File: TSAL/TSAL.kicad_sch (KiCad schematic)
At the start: 111 parts, among them IC1 ISO224ADWVR, IC2 ISO224ADWVR, IC3 LTC6995IS6-2#TRMPBF, IC4 LTC6995IS6-2#TRMPBF, J1 Conn_SDC, J2 Conn_TSAL, J3 Conn_AIR, J4 Conn_01x02, J5 Conn_VI, J6 Conn_Control, J7 Conn_HV, J8 Conn_Pre, K1 G2RL-2, Q1 ZXM61N02F, Q2 ZXM61N02F, Q3 ZXM61N02F, Q4 ZXM61N02F, Q5 IXTA6N100D2, U3 TLV7041DBV, U4 TLV7041DBV, U5 74LVC1G08, U6 AP2205-W5-7, U7 AP2205-W5-7, U9 AP2204K-ADJ

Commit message: feat: change iso OPA type and preC. circuit
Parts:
- removed C11: 0.1u, Capacitor_SMD:C_0603_1608Metric, symbol Device:C
- removed C12, C5: 0.22u, Capacitor_SMD:C_0603_1608Metric, symbol Device:C_Small
- removed C13, C18: 0.1u, Capacitor_SMD:C_0603_1608Metric, symbol Device:C_Small
- removed C14, C15, C19, C33: 1u, Capacitor_SMD:C_0603_1608Metric, symbol Device:C_Small
- removed D2: 1SS355VM, Diode_SMD:D_SOD-323F, symbol Diode:1SS355VM
- removed D3: BYG10J, Diode_SMD:D_SMA, symbol Device:D_Zener
- removed IC1, IC2: ISO224ADWVR, Package_SO:SOIC-8_7.5x5.85mm_P1.27mm, symbol ISO224ADWVR:ISO224ADWVR
- removed Q5: IXTA6N100D2, Package_TO_SOT_THT:TO-247-3_Vertical, symbol PCM_Transistor_MOSFET_AKL:IXTA6N100D2
- removed RV2, RV4: 10K, Potentiometer_THT:Potentiometer_Bourns_3296W_Vertical, symbol Device:R_Potentiometer
- removed TP3, TP9: TestPoint, TestPoint:TestPoint_THTPad_D1.5mm_Drill0.7mm, symbol Connector:TestPoint
- added C1, C3: 330p, Capacitor_SMD:C_0603_1608Metric, symbol Device:C_Small
- added C4: 1n, Capacitor_SMD:C_0603_1608Metric, symbol Device:C
- added C5: 1u, Capacitor_SMD:C_0603_1608Metric, symbol Device:C
- added D2: 1N4148W, Diode_SMD:D_SOD-123, symbol Diode:1N4148W
- added D3: S1J, Diode_SMD:D_SMA, symbol PCM_Diode_AKL:S1J
- added F2: 0ACJ-2000-TE, BelFuse:0ACJ, symbol Device:Fuse
- added Q5: DN2470K4, Package_TO_SOT_SMD:TO-252-2, symbol PCM_Transistor_MOSFET_AKL:DN2470K4
- added R1, R2, R3, R4: 3k3, Resistor_SMD:R_0603_1608Metric, symbol Device:R
- added R39, R46, R47, R48, R7: 1M, Resistor_SMD:R_0603_1608Metric, symbol Device:R
- added R5: 100k, Resistor_SMD:R_0603_1608Metric, symbol Device:R
- added TP1: TestPoint, TestPoint:TestPoint_THTPad_D1.5mm_Drill0.7mm, symbol Connector:TestPoint
- added U1, U8: AMC1351, Package_SO:SOIC-8_7.5x5.85mm_P1.27mm, symbol Amplifier_Difference:AMC1100DWV
- added U10, U2: TLV7041DBV, Package_TO_SOT_SMD:SOT-23-5, symbol Comparator:TLV7041DBV
- C10: value 1u -> 0.1u
- C8: value 0.22u -> 1n
- C9: value 0.22u -> 0.1u
- J6: value Conn_Control -> Conn_PRE
- J8: value Conn_Pre -> Conn_control
- Q1, Q2, Q3, Q4: value ZXM61N02F -> 2N7002
- R12, R15: value 82K -> 40k
- R13: value 5.1 -> 20k
- R17: value 5.1 -> 37k
- R20: value 1k -> 3k3
- R22, R23, R24: value 1k -> 1M
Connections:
- net +5V: now also R7.1, U1.8 (V+), U2.5 (V+), U8.8 (V+); no longer R23.1
- net +5VA: now also C9.1, C5.1, U1.1 (V+), U10.5 (V+), U8.1 (V+)
- net BATT+: now also F2.2, R39.1; no longer D10.2 (A), J7.4 (Pin_4)
- net GND1: now also R17.2, C4.2, C5.2, U1.3 (-), U1.4 (V-), U10.2 (V-), U8.3 (-), U8.4 (V-)
- net GND2: now also R24.1, C3.2, R4.1, R5.1, U1.5 (V-), U2.2 (V-), U8.5 (V-)
- net SDC: now also D2.1 (K)
- net at U3.3 (+): now also C1.1, R3.2, TP1.1, U2.1; no longer R20.1
- net at TP8.1, U4.1, U5.1: no longer R23.2
- net at J5.1 (Pin_1), R6.1, RV3.2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: now also Q5.1 (G)
- net at D4.2 (A): now also Q5.2 (D)
- net at RV3.1: now also Q5.3 (S)
- net at R21.2, TP7.1, U3.1: no longer R22.2
- net at U4.3 (+): now also R20.2; no longer R24.1
- net at U4.4 (-): now also R22.2, R23.2
- net at R15.2: now also R19.2, U10.3 (+); no longer R17.1
- net at J7.3 (Pin_3): now also D3.2 (A)
- net at R24.2: now also R23.1
- net at U3.4 (-): now also R13.2, R7.2
- net at R12.2: now also C8.1, R11.2, U1.2 (+); no longer R13.1
- net at K1.A2, Q2.3 (D): now also D2.2 (A)
- net BATT-: no longer names the net of D1.1 (K), J7.1 (Pin_1)
- new net: C3.1, R1.2, R4.2, U2.3 (+)
- new net: D3.1 (K), F2.1
- new net: C1.2, R2.2, R3.1, U2.4 (-)
- new net: R46.2, R47.1
- new net: R47.2, R48.1
- new net: D10.2 (A), J7.4 (Pin_4)
- new net: R39.2, R46.1
- new net: R2.1, U1.6 (-)
- new net: R1.1, U1.7 (+)
- new net: C4.1, U10.1, U8.2 (+)
- new net: R20.1, U8.7 (+)
- new net: R17.1, R48.2, U10.4 (-)
- new net: R13.1, R5.2
- no-connect marks 9 -> 8
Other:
- note added: "All resistors accuracy inside must within 1%."
- note added: "Rin=4.039M ->"
- note added: "Rin_{OPA}=1.25M"
- note removed: "Rin=1.25M"
- note removed: "Rtotal=87333"
- moved on the sheet: C17, C21, C6, C7, C8, D6, J2, J4, Q1, R10, R11, R12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

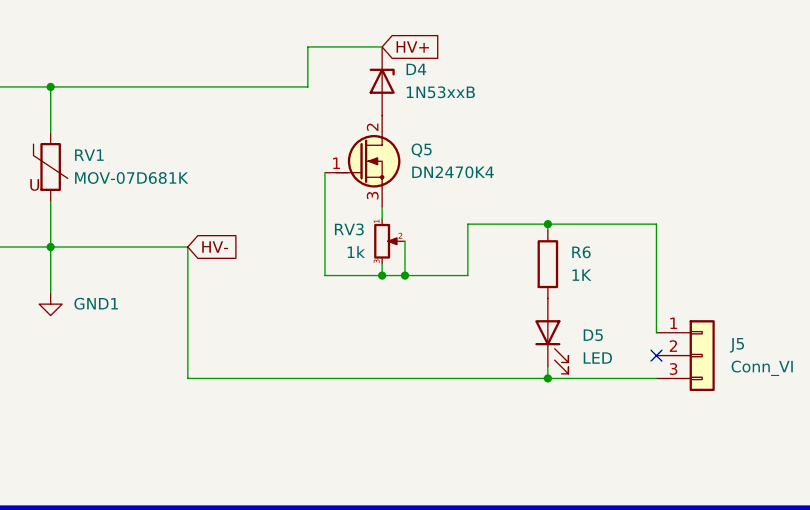
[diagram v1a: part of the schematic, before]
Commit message: fix: optimize VI schematics
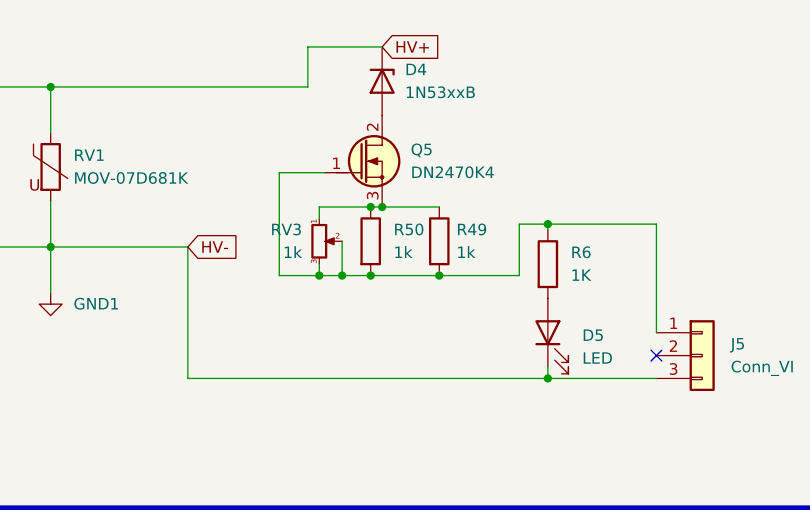
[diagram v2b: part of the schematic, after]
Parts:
- added R49, R50: 1k, Resistor_SMD:R_0805_2012Metric, symbol Device:R
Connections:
- net at J5.1 (Pin_1), Q5.1 (G), R6.1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: now also R49.2, R50.2
- net at Q5.3 (S), RV3.1: now also R49.1, R50.1
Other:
- moved on the sheet: RV3
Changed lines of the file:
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@@
   (junction (at 99.06 121.285) (diameter 0) (color 0 0 0 0)
   )
+  (junction (at 264.16 55.88) (diameter 0) (color 0 0 0 0)
+  )
   (junction (at 354.965 207.645) (diameter 0) (color 0 0 0 0)
   )
@@
   (junction (at 281.305 278.765) (diameter 0) (color 0 0 0 0)
   )
+  (junction (at 270.51 63.5) (diameter 0) (color 0 0 0 0)
+  )
   (junction (at 184.785 171.45) (diameter 0) (color 0 0 0 0)
   )
   (junction (at 176.53 141.605) (diameter 0) (color 0 0 0 0)
   )
+  (junction (at 262.89 55.88) (diameter 0) (color 0 0 0 0)
+  )
   (junction (at 140.335 205.74) (diameter 0) (color 0 0 0 0)
   )
@@
   (junction (at 218.44 172.085) (diameter 0) (color 0 0 0 0)
   )
-  (junction (at 266.7 63.5) (diameter 0) (color 0 0 0 0)
-  )
-  (junction (at 264.16 63.5) (diameter 0) (color 0 0 0 0)
+  (junction (at 257.175 63.5) (diameter 0) (color 0 0 0 0)
   )
   (junction (at 128.905 161.925) (diameter 0) (color 0 0 0 0)
@@
   (junction (at 259.08 217.805) (diameter 0) (color 0 0 0 0)
   )
+  (junction (at 259.715 63.5) (diameter 0) (color 0 0 0 0)
+  )
   (junction (at 100.965 161.925) (diameter 0) (color 0 0 0 0)
   )
@@
   (junction (at 99.695 217.805) (diameter 0) (color 0 0 0 0)
   )
+  (junction (at 262.89 63.5) (diameter 0) (color 0 0 0 0)
+  )
   (junction (at 219.71 120.015) (diameter 0) (color 0 0 0 0)
   )
@@
     (stroke (width 0) (type default))
   )
-  (wire (pts (xy 264.16 63.5) (xy 266.7 63.5))
+  (wire (pts (xy 259.715 63.5) (xy 262.89 63.5))
     (stroke (width 0) (type default))
   )
@@
     (stroke (width 0) (type default))
   )
+  (wire (pts (xy 270.51 63.5) (xy 279.4 63.5))
+    (stroke (width 0) (type default))
+  )
   (wire (pts (xy 218.44 172.085) (xy 218.44 167.005))
     (stroke (width 0) (type default))
@@
     (stroke (width 0) (type default))
   )
+  (wire (pts (xy 257.175 55.88) (xy 262.89 55.88))
+    (stroke (width 0) (type default))
+  )
   (wire (pts (xy 100.965 161.925) (xy 100.965 172.72))
     (stroke (width 0) (type default))
@@
     (stroke (width 0) (type default))
   )
+  (wire (pts (xy 257.175 63.5) (xy 259.715 63.5))
+    (stroke (width 0) (type default))
+  )
   (wire (pts (xy 187.96 276.86) (xy 187.96 278.13))
     (stroke (width 0) (type default))
@@
     (stroke (width 0) (type default))
   )
+  (wire (pts (xy 264.16 55.88) (xy 270.51 55.88))
+    (stroke (width 0) (type default))
+  )
   (wire (pts (xy 178.435 278.13) (xy 187.96 278.13))
     (stroke (width 0) (type default))
@@
     (stroke (width 0) (type default))
   )
-  (wire (pts (xy 264.16 63.5) (xy 264.16 62.23))
+  (wire (pts (xy 257.175 63.5) (xy 257.175 62.23))
     (stroke (width 0) (type default))
   )
@@
     (stroke (width 0) (type default))
   )
-  (wire (pts (xy 266.7 59.69) (xy 266.7 63.5))
+  (wire (pts (xy 262.89 63.5) (xy 270.51 63.5))
+    (stroke (width 0) (type default))
+  )
+  (wire (pts (xy 259.715 59.69) (xy 259.715 63.5))
     (stroke (width 0) (type default))
   )
@@
     (stroke (width 0) (type default))
   )
-  (wire (pts (xy 273.685 57.785) (xy 273.685 63.5))
+  (wire (pts (xy 279.4 57.785) (xy 279.4 63.5))
     (stroke (width 0) (type default))
   )
@@
     (stroke (width 0) (type default))
   )
-  (wire (pts (xy 257.81 63.5) (xy 264.16 63.5))
+  (wire (pts (xy 252.73 63.5) (xy 257.175 63.5))
     (stroke (width 0) (type default))
   )
@@
     (stroke (width 0) (type default))
   )
+  (wire (pts (xy 252.73 52.07) (xy 257.81 52.07))
+    (stroke (width 0) (type default))
+  )
   (wire (pts (xy 337.185 257.175) (xy 337.185 272.415))
     (stroke (width 0) (type default))
@@
     (stroke (width 0) (type default))
   )
-  (wire (pts (xy 266.7 63.5) (xy 273.685 63.5))
-    (stroke (width 0) (type default))
-  )
   (wire (pts (xy 165.1 275.59) (xy 165.1 278.13))
     (stroke (width 0) (type default))
@@
     (stroke (width 0) (type default))
   )
-  (wire (pts (xy 273.685 57.785) (xy 282.575 57.785))
+  (wire (pts (xy 279.4 57.785) (xy 282.575 57.785))
     (stroke (width 0) (type default))
   )
@@
     (stroke (width 0) (type default))
   )
-  (wire (pts (xy 264.16 57.15) (xy 264.16 55.88))
+  (wire (pts (xy 257.175 57.15) (xy 257.175 55.88))
     (stroke (width 0) (type default))
   )
@@
     (stroke (width 0) (type default))
   )
+  (wire (pts (xy 262.89 55.88) (xy 264.16 55.88))
+    (stroke (width 0) (type default))
+  )
   (wire (pts (xy 173.99 167.005) (xy 175.26 167.005))
     (stroke (width 0) (type default))
@@
     (stroke (width 0) (type default))
   )
-  (wire (pts (xy 257.81 52.07) (xy 257.81 63.5))
+  (wire (pts (xy 252.73 52.07) (xy 252.73 63.5))
     (stroke (width 0) (type default))
   )
@@
     )
   )
+  (symbol (lib_id "Device:R") (at 270.51 59.69 0) (unit 1)
+    (in_bom yes) (on_board yes) (dnp no) (fields_autoplaced)
+    (property "Reference" "R49" (at 272.415 58.42 0)
+      (effects (font (size 1.27 1.27)) (justify left))
+    )
+    (property "Value" "1k" (at 272.415 60.96 0)
+      (effects (font (size 1.27 1.27)) (justify left))
+    )
+    (property "Footprint" "Resistor_SMD:R_0805_2012Metric" (at 268.732 59.69 90)
+      (effects (font (size 1.27 1.27)) hide)
+    )
+    (property "Datasheet" "~" (at 270.51 59.69 0)
+      (effects (font (size 1.27 1.27)) hide)
+    )
+    (pin "1")
+    (pin "2")
+    (instances
+      (project "TSAL"
+        (path "/89b78632-2ae8-4b6b-a96e-85b5cad19713"
+          (reference "R49") (unit 1)
+        )
+      )
+    )
+  )
   (symbol (lib_id "power:GND2") (at 182.245 114.935 0) (unit 1)
     (in_bom yes) (on_board yes) (dnp no) (fields_autoplaced)
@@
     )
   )
+  (symbol (lib_id "Device:R") (at 262.89 59.69 0) (unit 1)
+    (in_bom yes) (on_board yes) (dnp no) (fields_autoplaced)
+    (property "Reference" "R50" (at 265.43 58.42 0)
+      (effects (font (size 1.27 1.27)) (justify left))
+    )
+    (property "Value" "1k" (at 265.43 60.96 0)
+      (effects (font (size 1.27 1.27)) (justify left))
+    )
+    (property "Footprint" "Resistor_SMD:R_0805_2012Metric" (at 261.112 59.69 90)
+      (effects (font (size 1.27 1.27)) hide)
+    )
+    (property "Datasheet" "~" (at 262.89 59.69 0)
+      (effects (font (size 1.27 1.27)) hide)
+    )
+    (pin "1")
+    (pin "2")
+    (instances
+      (project "TSAL"
+        (path "/89b78632-2ae8-4b6b-a96e-85b5cad19713"
+          (reference "R50") (unit 1)
+        )
+      )
+    )
+  )
   (symbol (lib_id "power:+5V") (at 205.74 210.185 0) (unit 1)
     (in_bom yes) (on_board yes) (dnp no) (fields_autoplaced)
@@
     )
   )
-  (symbol (lib_id "Device:R_Potentiometer_Small") (at 264.16 59.69 0) (unit 1)
+  (symbol (lib_id "Device:R_Potentiometer_Small") (at 257.175 59.69 0) (unit 1)
     (in_bom yes) (on_board yes) (dnp no)
-    (property "Reference" "RV3" (at 262.255 58.42 0)
+    (property "Reference" "RV3" (at 255.27 58.42 0)
       (effects (font (size 1.27 1.27)) (justify right))
     )
-    (property "Value" "1k" (at 262.255 60.96 0)
+    (property "Value" "1k" (at 255.27 60.96 0)
       (effects (font (size 1.27 1.27)) (justify right))
     )
-    (property "Footprint" "Potentiometer_THT:Potentiometer_Bourns_3296W_Vertical" (at 264.16 59.69 0)
+    (property "Footprint" "Potentiometer_THT:Potentiometer_Bourns_3296W_Vertical" (at 257.175 59.69 0)
       (effects (font (size 1.27 1.27)) hide)
     )
-    (property "Datasheet" "~" (at 264.16 59.69 0)
+    (property "Datasheet" "~" (at 257.175 59.69 0)
       (effects (font (size 1.27 1.27)) hide)
     )

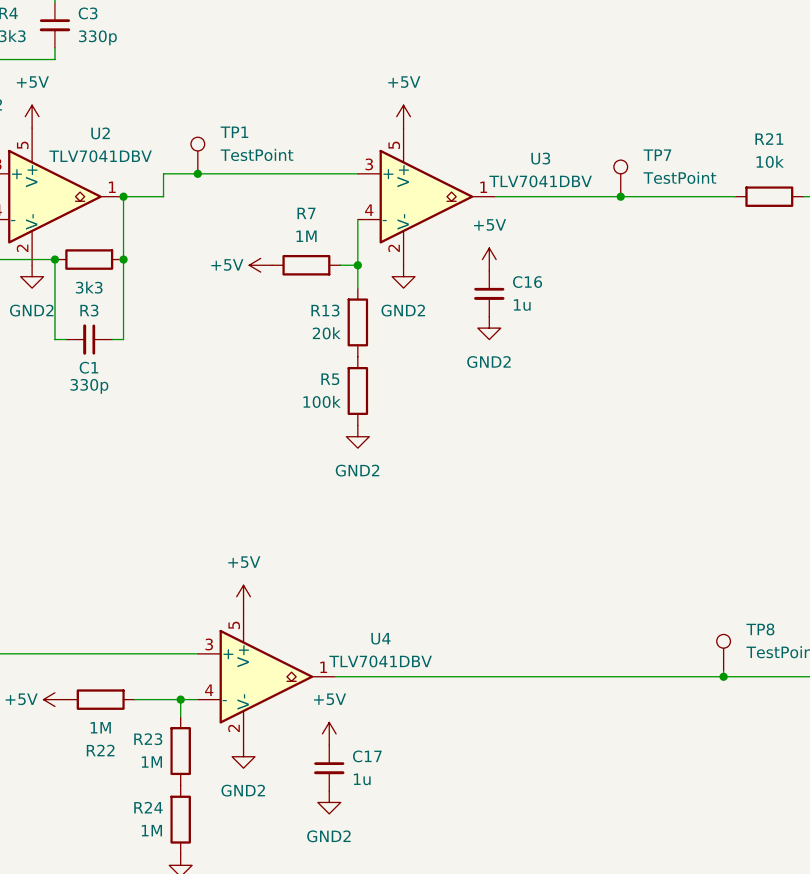
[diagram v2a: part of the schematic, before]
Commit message: change comparator
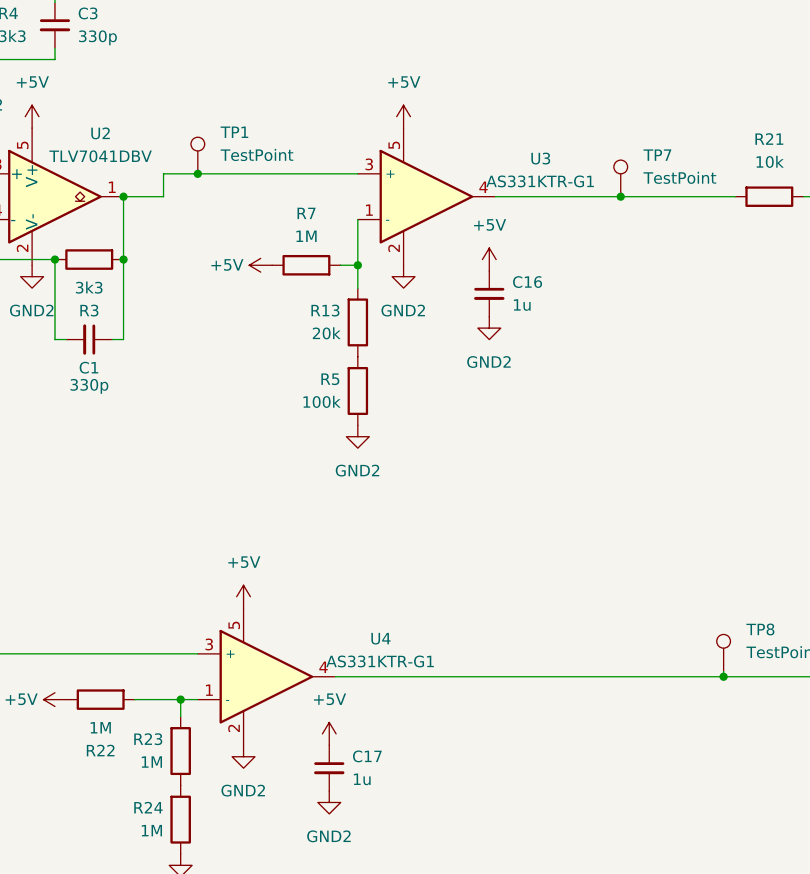
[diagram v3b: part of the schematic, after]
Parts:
- removed U3, U4: TLV7041DBV, Package_TO_SOT_SMD:SOT-23-5, symbol Comparator:TLV7041DBV
- added U3, U4: AS331KTR-G1, Package_TO_SOT_SMD:SOT-23-5, symbol Project_Lib:AS331KTR-G1
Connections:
- net +5V: now also U3.5, U4.5
- net GND2: now also U3.2, U4.2
- net at R13.2, R7.2: now also U3.1 (-)
- net at C1.1, R3.2, TP1.1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: now also U3.3 (+)
- net at TP8.1, U5.1: now also U4.4
- net at R20.2: now also U4.3 (+)
- net at R22.2, R23.2: now also U4.1 (-)
- net at R21.2, TP7.1: now also U3.4
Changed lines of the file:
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@@
 (kicad_sch (version 20230121) (generator eeschema)
   (paper "A2")
+  (title_block
+    (date "2025-08-03")
+    (rev "v2025.08")
+  )
   (junction (at 212.09 109.855) (diameter 0) (color 0 0 0 0)
   )
@@
     )
   )
+  (symbol (lib_id "Project_Lib:AS331KTR-G1") (at 223.52 164.465 0) (unit 1)
+    (in_bom yes) (on_board yes) (dnp no) (fields_autoplaced)
+    (property "Reference" "U3" (at 238.76 160.2741 0)
+      (effects (font (size 1.27 1.27)))
+    )
+    (property "Value" "AS331KTR-G1" (at 238.76 162.8141 0)
+      (effects (font (size 1.27 1.27)))
+    )
+    (property "Footprint" "Package_TO_SOT_SMD:SOT-23-5" (at 232.41 180.975 0)
+      (effects (font (size 1.27 1.27)) hide)
+    )
+    (property "Datasheet" "https://www.mouser.tw/datasheet/2/115/AS331-3213702.pdf" (at 218.44 178.435 0)
+      (effects (font (size 1.27 1.27)) hide)
+    )
+    (pin "1")
+    (pin "3")
+    (pin "5")
+    (pin "4")
+    (pin "2")
+    (instances
+      (project "TSAL"
+        (path "/89b78632-2ae8-4b6b-a96e-85b5cad19713"
+          (reference "U3") (unit 1)
+        )
+      )
+    )
+  )
   (symbol (lib_id "power:GND2") (at 288.925 295.275 0) (unit 1)
     (in_bom yes) (on_board yes) (dnp no) (fields_autoplaced)
@@
     )
   )
-  (symbol (lib_id "Comparator:TLV7041DBV") (at 208.28 217.805 0) (unit 1)
-    (in_bom yes) (on_board yes) (dnp no) (fields_autoplaced)
-    (property "Reference" "U4" (at 220.98 213.6141 0)
-      (effects (font (size 1.27 1.27)))
-    )
-    (property "Value" "TLV7041DBV" (at 220.98 216.1541 0)
-      (effects (font (size 1.27 1.27)))
-    )
-    (property "Footprint" "Package_TO_SOT_SMD:SOT-23-5" (at 208.28 227.965 0)
-      (effects (font (size 1.27 1.27)) hide)
-    )
-    (property "Datasheet" "https://www.ti.com/lit/ds/symlink/tlv7041.pdf" (at 208.28 217.805 0)
-      (effects (font (size 1.27 1.27)) hide)
-    )
-    (pin "5")
-    (pin "1")
-    (pin "3")
-    (pin "4")
-    (pin "2")
-    (instances
-      (project "TSAL"
-        (path "/89b78632-2ae8-4b6b-a96e-85b5cad19713"
-          (reference "U4") (unit 1)
-        )
-      )
-    )
-  )
   (symbol (lib_id "power:GND2") (at 219.71 120.015 0) (unit 1)
     (in_bom yes) (on_board yes) (dnp no) (fields_autoplaced)
@@
     )
   )
+  (symbol (lib_id "Project_Lib:AS331KTR-G1") (at 205.74 217.805 0) (unit 1)
+    (in_bom yes) (on_board yes) (dnp no) (fields_autoplaced)
+    (property "Reference" "U4" (at 220.98 213.6141 0)
+      (effects (font (size 1.27 1.27)))
+    )
+    (property "Value" "AS331KTR-G1" (at 220.98 216.1541 0)
+      (effects (font (size 1.27 1.27)))
+    )
+    (property "Footprint" "Package_TO_SOT_SMD:SOT-23-5" (at 214.63 234.315 0)
+      (effects (font (size 1.27 1.27)) hide)
+    )
+    (property "Datasheet" "https://www.mouser.tw/datasheet/2/115/AS331-3213702.pdf" (at 200.66 231.775 0)
+      (effects (font (size 1.27 1.27)) hide)
+    )
+    (pin "1")
+    (pin "3")
+    (pin "5")
+    (pin "4")
+    (pin "2")
+    (instances
+      (project "TSAL"
+        (path "/89b78632-2ae8-4b6b-a96e-85b5cad19713"
+          (reference "U4") (unit 1)
+        )
+      )
+    )
+  )
   (symbol (lib_id "power:+5V") (at 155.575 210.185 270) (unit 1)
     (in_bom yes) (on_board yes) (dnp no) (fields_autoplaced)
@@
         )
       )
-    )
-  )
-  (symbol (lib_id "Comparator:TLV7041DBV") (at 226.06 164.465 0) (unit 1)
-    (in_bom yes) (on_board yes) (dnp no) (fields_autoplaced)
-    (property "Reference" "U3" (at 238.76 160.2741 0)
-      (effects (font (size 1.27 1.27)))
-    )
-    (property "Value" "TLV7041DBV" (at 238.76 162.8141 0)
-      (effects (font (size 1.27 1.27)))
-    )
-    (property "Footprint" "Package_TO_SOT_SMD:SOT-23-5" (at 226.06 174.625 0)
-      (effects (font (size 1.27 1.27)) hide)
-    )
-    (property "Datasheet" "https://www.ti.com/lit/ds/symlink/tlv7041.pdf" (at 226.06 164.465 0)
-      (effects (font (size 1.27 1.27)) hide)
-    )
-    (pin "5")
-    (pin "1")
-    (pin "3")
-    (pin "4")
-    (pin "2")
-    (instances
-      (project "TSAL"
-        (path "/89b78632-2ae8-4b6b-a96e-85b5cad19713"
-          (reference "U3") (unit 1)
-        )
-      )
